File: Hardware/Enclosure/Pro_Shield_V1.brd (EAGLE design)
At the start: 58.4 x 58.4 mm, 9 parts, among them J1 ARDUINO_R3_SHIELD

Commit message: Updating EAGLE files
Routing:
- net MOSI: track 46.2 -> 48.7 mm
- net MISO: track 56.9 -> 58.7 mm
- net RST: track 70.9 -> 69.4 mm
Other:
- board size 58.4 x 58.4 mm -> 59.7 x 58.4 mm

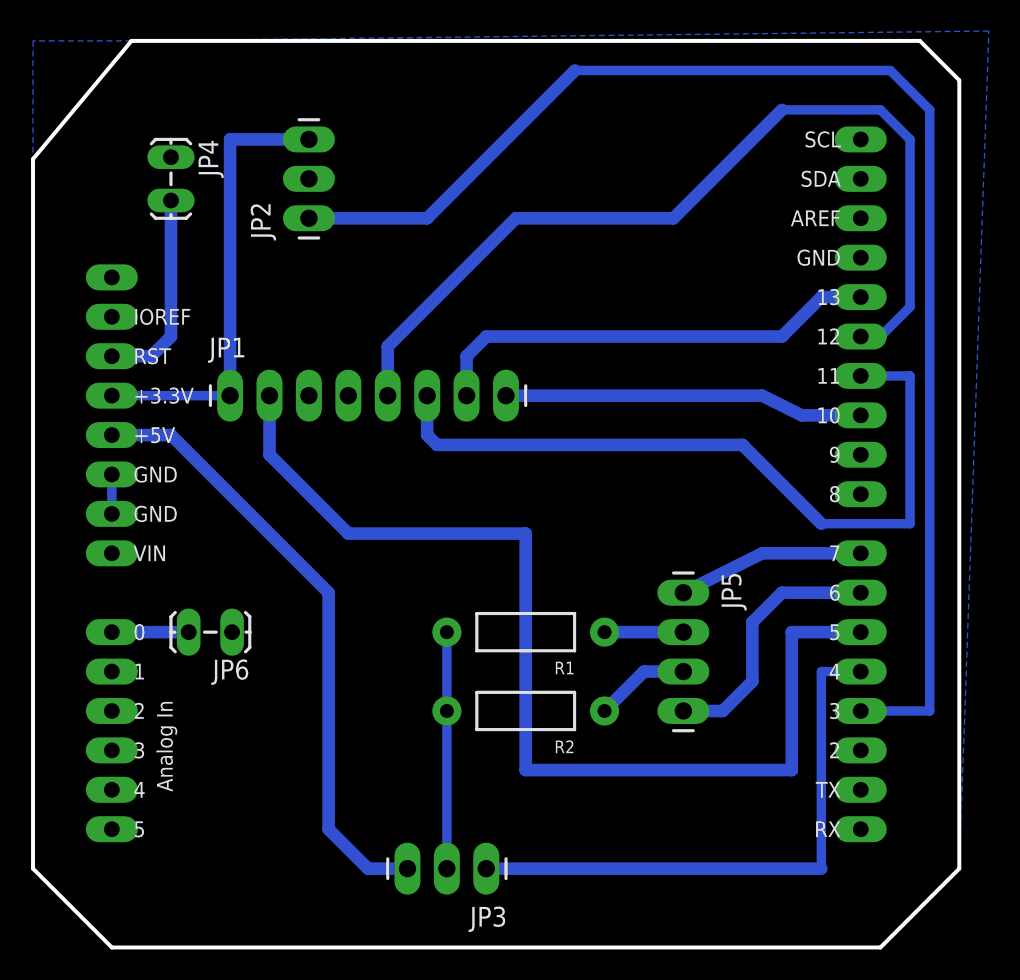
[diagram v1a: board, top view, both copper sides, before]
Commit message: New boards, terminal enclosures, and labview interface
Former-commit-id: 246ca6c8f016e846ca299188d99d46875b994b37
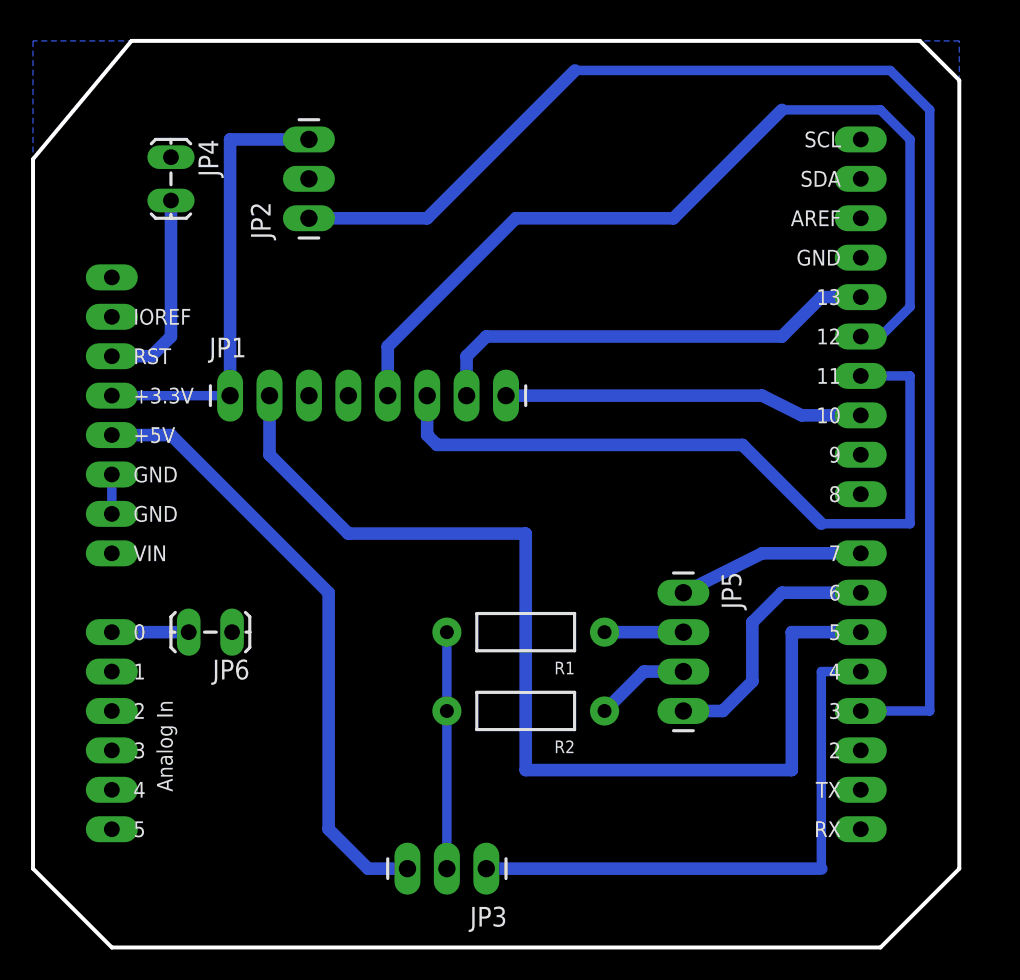
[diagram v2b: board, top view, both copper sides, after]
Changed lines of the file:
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@@
 <wire x1="3.81" y1="27.94" x2="3.81" y2="30.48" width="0.6096" layer="16"/>
 <polygon width="0.6096" layer="16" isolate="0.8128" thermals="no">
-<vertex x="60.325" y="59.055"/>
-<vertex x="5.08" y="58.42"/>
+<vertex x="58.42" y="58.42"/>
 <vertex x="-1.27" y="58.42"/>
 <vertex x="-1.27" y="5.08"/>
